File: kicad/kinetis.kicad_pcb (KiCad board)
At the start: 2 copper layers, 88.9 x 88.9 mm, 75 parts, among them J1 FTDI_Connector, J2 CONN_01X16, J3 USB_Micro_B, J4 CONN_01X16, J5 JLink_SWD_20pin, J6 CONN_01X16, J7 CONN_01X16, M1 #4-40 Mounting Hole, M2 #4-40 Mounting Hole, M3 #4-40 Mounting Hole, M4 #4-40 Mounting Hole, SW1 DPDT, SW2 SPST, SW3 SPST, SW4 SPST, SW5 SPST, SW6 SPST, U1 LM1117-ADJ, U2 MKL16Z64VLH4, Y1 12.000 MHz

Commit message: Misc tweaks
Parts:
- added C17: 0.1uF, custom_footprints:SM_0603, F.Cu at (160.8, 129.5)
- added C18: 0.1uF, custom_footprints:SM_0603, F.Cu at (172.8, 84.6)
- added C8: 0.1uF, custom_footprints:SM_0603, F.Cu at (126.8, 89.7)
- renumbered C9 to C10, C10 to C11, C11 to C12, C12 to C13, C13 to C14, C14 to C15, C15 to C16, C16 to C19, C17 to C20, C8 to C9
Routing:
- net GND: track 144.6 -> 157.0 mm, vias 53 -> 54
- net +3.3V: track 323.1 -> 334.2 mm
- net Net-(F1-Pad2): track 17.3 -> 16.4 mm
- net /HEADER_A[2]: track 24.0 -> 24.8 mm

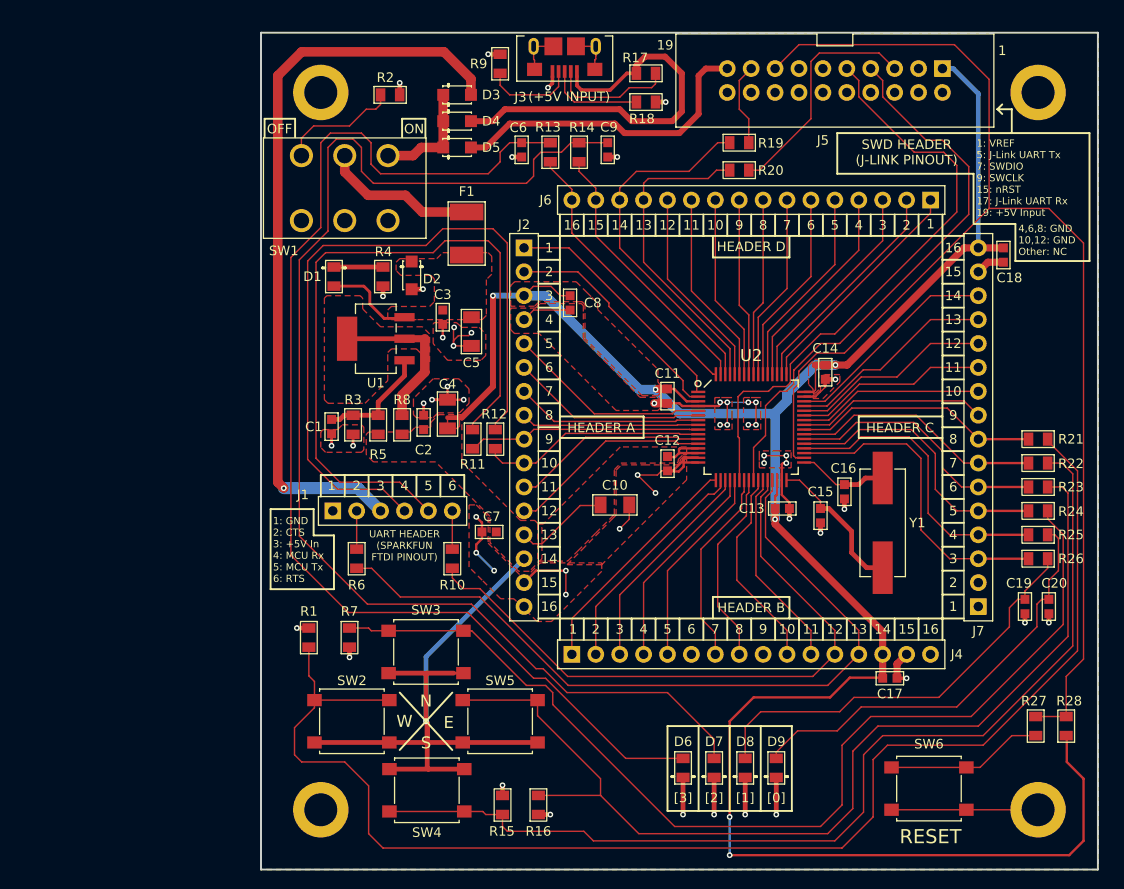
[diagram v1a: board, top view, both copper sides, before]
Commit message: Cosmetic tweaks. Added copper thieving.
This commit adds ground-referenced copper thieving to the top layer
of the PCB, and also makes a whole bunch of cosmetic changes, including
a logo on the PCB and schematic, and infoblocks for the CCA and PCB.
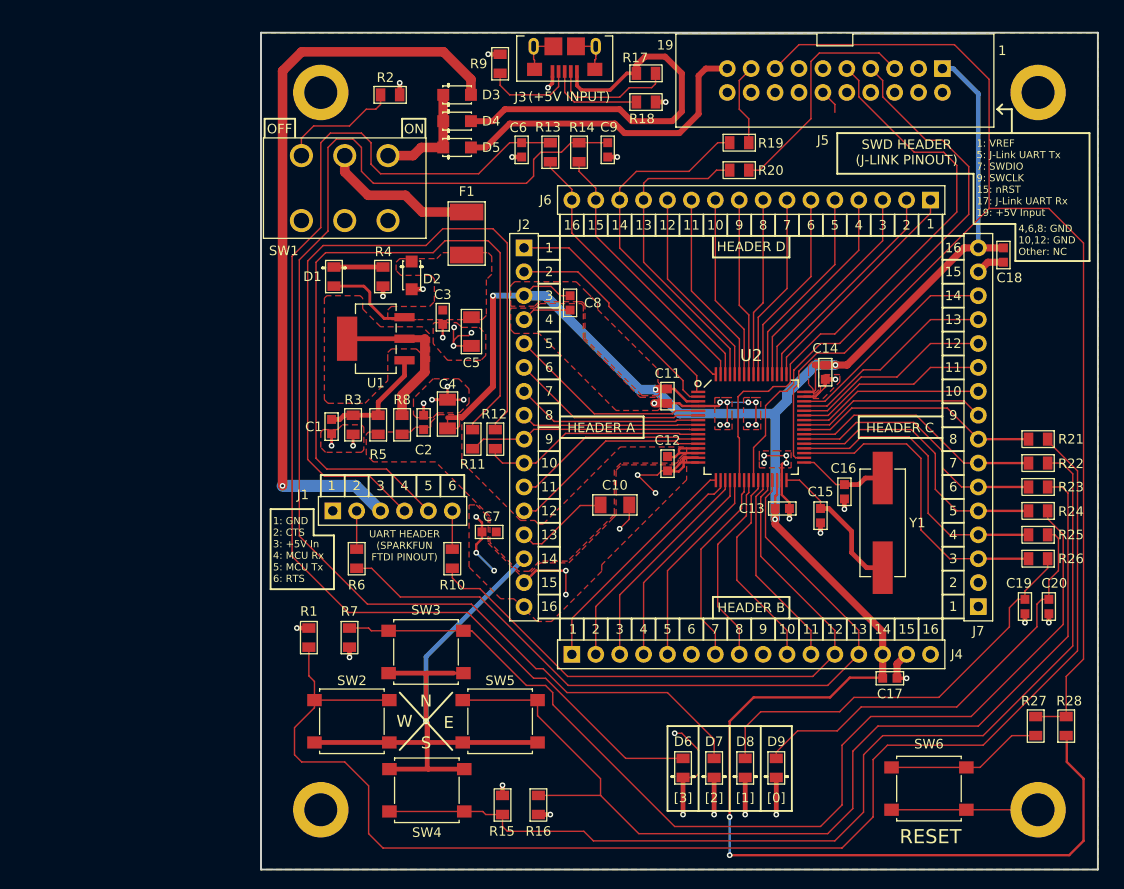
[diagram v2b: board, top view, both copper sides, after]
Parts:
- added G***: Hoboshop, custom_footprints:Hoboshop, B.Cu at (107.3, 98.4)
- added REF**: CCA_TITLE_BLOCK, custom_footprints:CCA_TITLE_BLOCK, B.Cu at (160.0, 95.9)
- added REF**: PCB_TITLE_BLOCK, custom_footprints:PCB_TITLE_BLOCK, B.Cu at (167.0, 75.6)
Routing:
- net GND: track 157.0 -> 168.4 mm, vias 54 -> 55
- net /LED[3]: track 125.6 -> 124.9 mm
- net +3.3V: track 334.2 -> 333.6 mm
- net 5V_FTDI: track 79.8 -> 79.3 mm
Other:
- rule pad_to_mask_clearance: 0.1016 -> 0.0508
- board text added: ""The Ripper" A Kinetis KL016 Evaluation Board"

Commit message: Various cosmetic tweaks
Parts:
- added G***: LOGO, custom_footprints:Signature_Mask, B.Cu at (112.5, 143.8)
- moved REF** 74.3 mm to (125.5, 137.2)
- moved REF** 38.4 mm to (172.7, 132.1)
- moved G*** 25.0 mm to (116.8, 75.3)
- moved J3 0.41 mm to (126.2, 62.8)
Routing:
- net 5V_USB: track 43.0 -> 22.5 mm
- net GND: track 168.4 -> 177.1 mm, vias 55 -> 57
- net Net-(J3-Pad2): track 12.6 -> 14.6 mm, vias 0 -> 2
- net Net-(J3-Pad3): track 9.75 -> 11.0 mm, vias 0 -> 2
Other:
- board text added: "01-001"
- board text added: "02-001"
- board text added: "1.0"
- board text added: "Flip the board over"

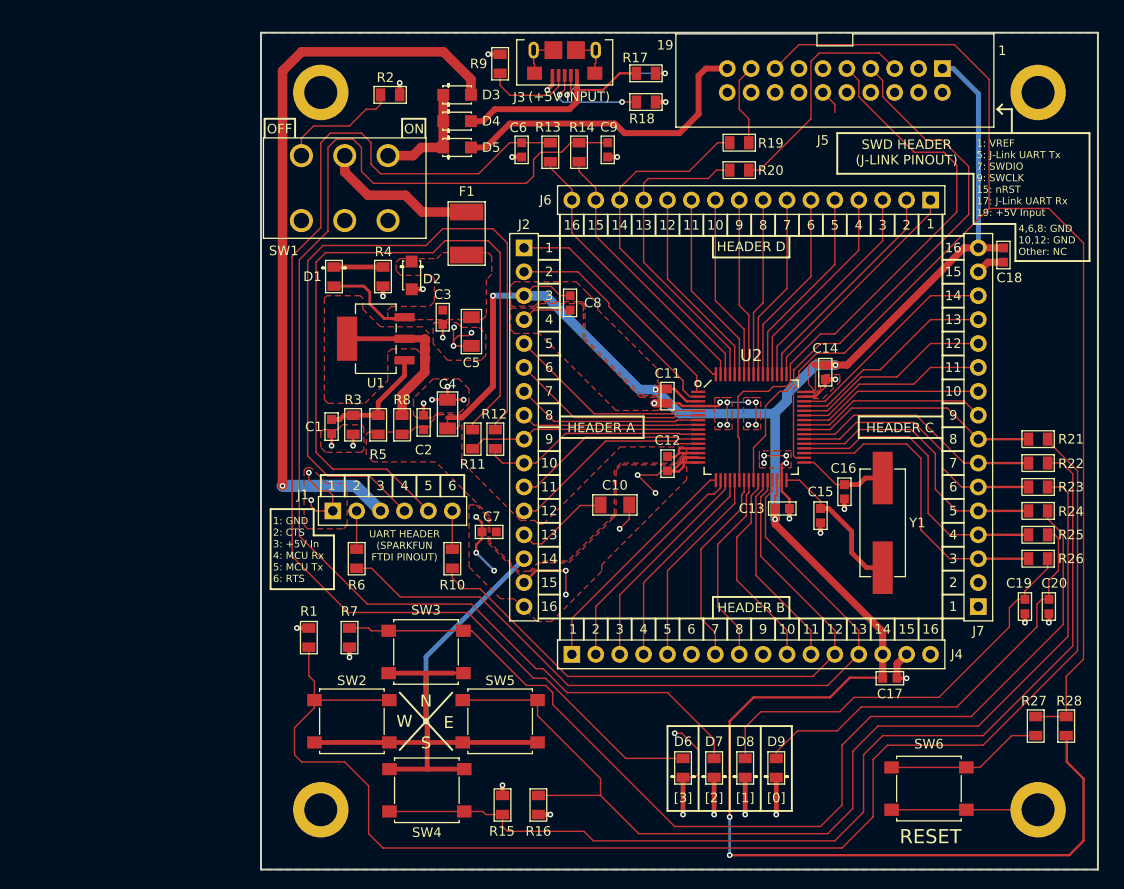
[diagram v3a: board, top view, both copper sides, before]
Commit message: Removed GND-fill pour from top side
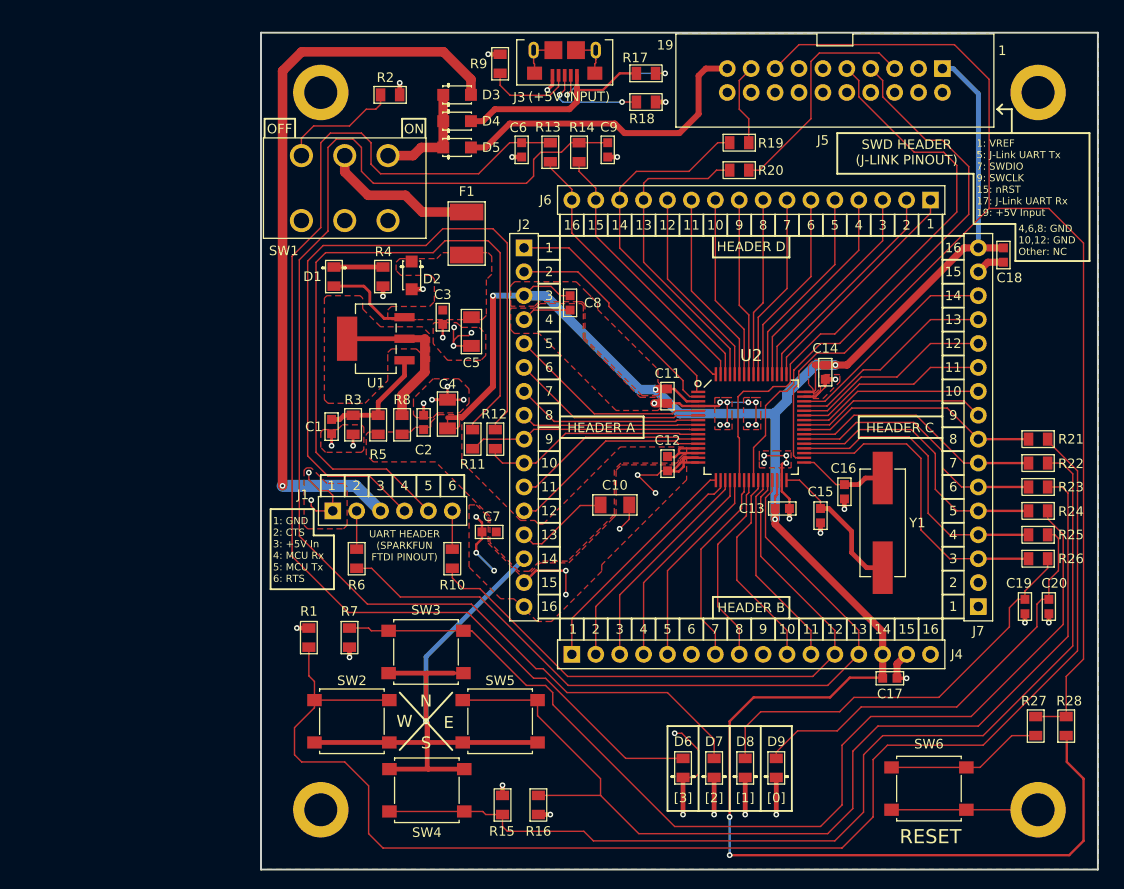
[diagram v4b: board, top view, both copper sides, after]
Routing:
- net GND: track 177.1 -> 174.5 mm
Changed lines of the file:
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@@
     (thickness 1.6002)
     (drawings 230)
-    (tracks 880)
+    (tracks 874)
     (zones 0)
     (modules 82)
@@
   (page A)
   (layers
-    (0 F.Cu signal hide)
+    (0 F.Cu signal)
     (31 B.Cu signal)
-    (33 F.Adhes user hide)
-    (35 F.Paste user hide)
+    (33 F.Adhes user)
+    (35 F.Paste user)
     (36 B.SilkS user)
-    (37 F.SilkS user hide)
+    (37 F.SilkS user)
     (38 B.Mask user)
-    (39 F.Mask user hide)
-    (40 Dwgs.User user hide)
-    (41 Cmts.User user hide)
-    (42 Eco1.User user hide)
-    (43 Eco2.User user hide)
-    (44 Edge.Cuts user hide)
-    (45 Margin user hide)
-    (47 F.CrtYd user hide)
-    (49 F.Fab user hide)
+    (39 F.Mask user)
+    (40 Dwgs.User user)
+    (41 Cmts.User user)
+    (42 Eco1.User user)
+    (43 Eco2.User user)
+    (44 Edge.Cuts user)
+    (45 Margin user)
+    (47 F.CrtYd user)
+    (49 F.Fab user)
   )
   (setup
-    (last_trace_width 0.1524)
+    (last_trace_width 0.254)
     (user_trace_width 0.1524)
     (user_trace_width 0.3048)
@@
   (gr_line (start 93.98 149.86) (end 93.98 60.96) (angle 90) (layer F.Fab) (width 0.2))
   (gr_line (start 182.88 149.86) (end 93.98 149.86) (angle 90) (layer F.Fab) (width 0.2))
-  (segment (start 124.693997 66.751191) (end 124.389198 67.05599) (width 0.381) (layer F.Cu) (net 1))
-  (segment (start 124.938 66.507188) (end 124.693997 66.751191) (width 0.381) (layer F.Cu) (net 1))
-  (segment (start 124.938 66.0164) (end 124.938 66.507188) (width 0.381) (layer F.Cu) (net 1))
+  (segment (start 124.938 66.507188) (end 124.389198 67.05599) (width 0.381) (layer F.Cu) (net 1))
+  (segment (start 124.938 66.0164) (end 124.938 66.507188) (width 0.381) (layer F.Cu) (net 1) (status 10))
   (via (at 124.389198 67.05599) (size 0.6096) (drill 0.3048) (layers F.Cu B.Cu) (net 1))
-  (segment (start 150.114 111.506) (end 150.114 110.49) (width 0.254) (layer F.Cu) (net 1))
+  (segment (start 150.114 111.506) (end 150.114 110.49) (width 0.254) (layer F.Cu) (net 1) (status 10))
   (segment (start 150.114 110.49) (end 149.3 109.676) (width 0.254) (layer F.Cu) (net 1))
-  (segment (start 149.3 109.676) (end 149.3 108.495) (width 0.254) (layer F.Cu) (net 1))
+  (segment (start 149.3 109.676) (end 149.3 108.495) (width 0.254) (layer F.Cu) (net 1) (status 20))
   (segment (start 99.822 111.76) (end 99.314 111.252) (width 0.1524) (layer F.Cu) (net 1))
   (segment (start 99.314 111.252) (end 99.314 110.617) (width 0.1524) (layer F.Cu) (net 1))
@@
   (segment (start 152.9068 99.62) (end 153.3652 99.1616) (width 0.1524) (layer F.Cu) (net 1))
   (segment (start 153.924 98.3488) (end 153.924 97.79) (width 0.254) (layer F.Cu) (net 1) (status 20))
-  (segment (start 154.94 68.58) (end 154.94 69.418948) (width 0.1524) (layer F.Cu) (net 1))
-  (segment (start 153.67 67.31) (end 154.94 68.58) (width 0.1524) (layer F.Cu) (net 1) (status 10))
   (segment (start 152.9068 99.62) (end 153.924 98.6028) (width 0.1524) (layer F.Cu) (net 1))
   (segment (start 153.924 98.6028) (end 153.924 97.79) (width 0.254) (layer F.Cu) (net 1) (status 20))
@@
   (segment (start 126.746 69.088) (end 118.8212 69.088) (width 0.635) (layer F.Cu) (net 10))
   (segment (start 118.8212 69.088) (end 117.5512 70.358) (width 0.635) (layer F.Cu) (net 10))
-  (segment (start 117.5512 70.358) (end 116.2812 70.358) (width 0.635) (layer F.Cu) (net 10))
+  (segment (start 117.5512 70.358) (end 116.2812 70.358) (width 0.635) (layer F.Cu) (net 10) (status 20))
   (segment (start 127.538 66.832) (end 127.546102 66.840102) (width 0.635) (layer F.Cu) (net 10))
   (segment (start 127.546102 66.840102) (end 127.546102 68.287898) (width 0.635) (layer F.Cu) (net 10))
   (segment (start 127.546102 68.287898) (end 126.746 69.088) (width 0.635) (layer F.Cu) (net 10))
-  (segment (start 133.858 65.278) (end 132.08 65.278) (width 0.254) (layer F.Cu) (net 10))
+  (segment (start 133.858 65.278) (end 132.08 65.278) (width 0.254) (layer F.Cu) (net 10) (status 10))
   (segment (start 132.08 65.278) (end 130.302 67.056) (width 0.254) (layer F.Cu) (net 10))
   (segment (start 130.302 67.056) (end 127.538 67.056) (width 0.254) (layer F.Cu) (net 10))
   (segment (start 127.538 67.056) (end 127.538 66.548) (width 0.254) (layer F.Cu) (net 10))
-  (segment (start 127.538 66.294) (end 127.538 66.548) (width 0.381) (layer F.Cu) (net 10))
+  (segment (start 127.538 65.4892) (end 127.538 66.548) (width 0.381) (layer F.Cu) (net 10) (status 10))
   (segment (start 127.538 66.548) (end 127.538 66.832) (width 0.381) (layer F.Cu) (net 10))
-  (segment (start 127.538 65.4892) (end 127.538 66.294) (width 0.381) (layer F.Cu) (net 10))
   (segment (start 104.013 109.093) (end 96.266 109.093) (width 1.27) (layer B.Cu) (net 11))
   (segment (start 106.68 111.76) (end 104.013 109.093) (width 1.27) (layer B.Cu) (net 11) (status 10))
@@
   (segment (start 130.81 66.548) (end 132.08 65.278) (width 0.1524) (layer B.Cu) (net 70))
   (segment (start 132.08 65.278) (end 136.906 65.278) (width 0.1524) (layer B.Cu) (net 70))
-  (segment (start 136.906 65.278) (end 135.89 65.278) (width 0.1524) (layer F.Cu) (net 70))
+  (segment (start 136.906 65.278) (end 135.89 65.278) (width 0.1524) (layer F.Cu) (net 70) (status 20))
   (via (at 136.906 65.278) (size 0.6096) (drill 0.3048) (layers F.Cu B.Cu) (net 70))
-  (segment (start 126.798231 67.260633) (end 126.493432 67.565432) (width 0.1524) (layer F.Cu) (net 70))
+  (segment (start 126.888 67.170864) (end 126.493432 67.565432) (width 0.1524) (layer F.Cu) (net 70))
   (via (at 126.493432 67.565432) (size 0.6096) (drill 0.3048) (layers F.Cu B.Cu) (net 70))
-  (segment (start 126.888 67.170864) (end 126.798231 67.260633) (width 0.1524) (layer F.Cu) (net 70))
-  (segment (start 126.888 65.4892) (end 126.888 67.170864) (width 0.1524) (layer F.Cu) (net 70))
+  (segment (start 126.888 65.4892) (end 126.888 67.170864) (width 0.1524) (layer F.Cu) (net 70) (status 10))
   (segment (start 125.704587 67.564) (end 125.704587 67.995052) (width 0.1524) (layer B.Cu) (net 71))
   (segment (start 125.704587 67.995052) (end 126.035535 68.326) (width 0.1524) (layer B.Cu) (net 71))
   (segment (start 126.035535 68.326) (end 132.334 68.326) (width 0.1524) (layer B.Cu) (net 71))
-  (segment (start 132.334 68.326) (end 133.858 68.326) (width 0.1524) (layer F.Cu) (net 71))
+  (segment (start 132.334 68.326) (end 133.858 68.326) (width 0.1524) (layer F.Cu) (net 71) (status 20))
   (via (at 132.334 68.326) (size 0.6096) (drill 0.3048) (layers F.Cu B.Cu) (net 71))
-  (segment (start 126.238 65.4892) (end 126.238 67.030587) (width 0.1524) (layer F.Cu) (net 71))
-  (segment (start 126.238 67.030587) (end 126.009386 67.259201) (width 0.1524) (layer F.Cu) (net 71))
-  (segment (start 126.009386 67.259201) (end 125.704587 67.564) (width 0.1524) (layer F.Cu) (net 71))
+  (segment (start 126.238 65.4892) (end 126.238 67.030587) (width 0.1524) (layer F.Cu) (net 71) (status 10))
+  (segment (start 126.238 67.030587) (end 125.704587 67.564) (width 0.1524) (layer F.Cu) (net 71))
   (via (at 125.704587 67.564) (size 0.6096) (drill 0.3048) (layers F.Cu B.Cu) (net 71))
-  (segment (start 119.38 65.278) (end 119.38 66.548) (width 0.1524) (layer F.Cu) (net 72))
+  (segment (start 119.38 65.278) (end 119.38 66.548) (width 0.1524) (layer F.Cu) (net 72) (status 10))
   (segment (start 119.38 66.548) (end 120.4468 67.6148) (width 0.1524) (layer F.Cu) (net 72))
   (segment (start 120.4468 67.6148) (end 124.6632 67.6148) (width 0.1524) (layer F.Cu) (net 72))
   (segment (start 124.6632 67.6148) (end 125.5945 66.6835) (width 0.1524) (layer F.Cu) (net 72))
-  (segment (start 125.5945 66.6835) (end 125.5945 66.0099) (width 0.1524) (layer F.Cu) (net 72))
+  (segment (start 125.5945 66.6835) (end 125.5945 66.0099) (width 0.1524) (layer F.Cu) (net 72) (status 20))
   (segment (start 104.14 111.76) (end 104.14 115.824) (width 0.1524) (layer F.Cu) (net 73) (status 30))
   (segment (start 118.872 103.124) (end 118.872 102.4636) (width 0.1524) (layer F.Cu) (net 74) (status 10))
@@
       )
     )
-  )
-  (zone (net 1) (net_name GND) (layer F.Cu) (hatch edge 0.508)
-    (connect_pads (clearance 0.762))
-    (min_thickness 0.254)
-    (fill yes (mode segment) (arc_segments 32) (thermal_gap 0.635) (thermal_bridge_width 0.508))
-    (polygon
-      (pts
-        (xy 182.88 60.96) (xy 182.88 149.86) (xy 93.98 149.86) (xy 93.98 60.96)
-      )
-    )

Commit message: Added some more copper. Changed vias to 0.014"/0.032".
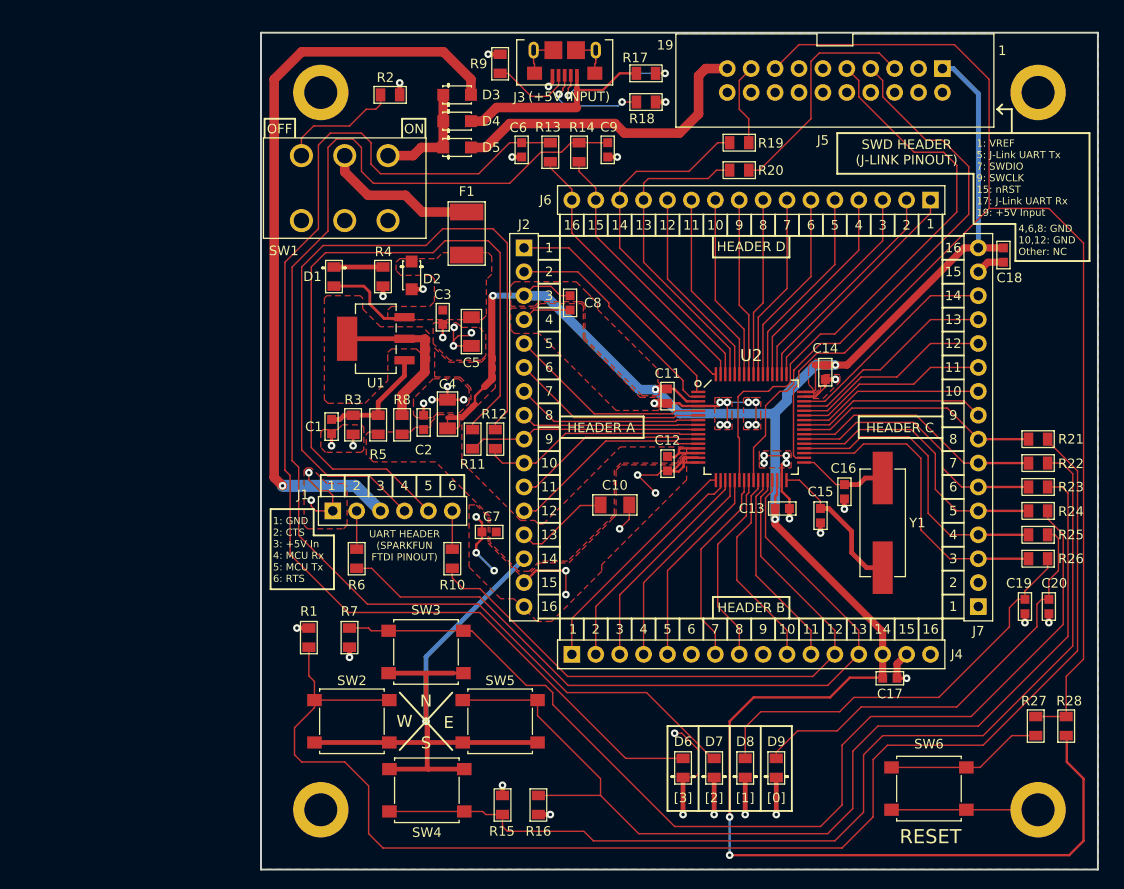
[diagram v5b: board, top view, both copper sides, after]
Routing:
- net /LED[2]: track 133.9 -> 132.3 mm
- net 5V_FTDI: track 79.3 -> 80.0 mm
- net Net-(J3-Pad4): track 8.99 -> 8.25 mm
- net /LED[3]: track 124.9 -> 125.6 mm
- net TXD_FTDI: track 77.0 -> 77.5 mm
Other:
- net class Default: via_dia 0.6096 -> 0.8128; via_drill 0.3048 -> 0.3556
- rule via_min_drill: 0.3048 -> 0.3556
- rule via_min_size: 0.6096 -> 0.8128

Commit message: Adde a shitload of copper
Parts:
- moved J5 1.80 mm to (165.1, 66.0)
- moved R19 0.76 mm to (144.8, 73.4)
- moved R17 0.51 mm to (134.4, 65.3)
- moved R18 0.51 mm to (134.4, 68.3)
- moved R20 0.23 mm to (144.8, 75.8)
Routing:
- net GND: track 174.0 -> 473.9 mm, vias 57 -> 89
- net (no net): track 0.00 -> 26.5 mm
- net 5V_JLink: track 33.9 -> 30.8 mm
- net Net-(J3-Pad2): track 14.5 -> 17.6 mm
- net JLink_nRST: track 142.7 -> 144.9 mm
- net JLink_SWCLK: track 63.4 -> 64.9 mm
- net Net-(J3-Pad3): track 11.5 -> 10.0 mm
- net JLink_SWDIO: track 60.1 -> 61.4 mm
- net RXD_FTDI: track 76.2 -> 75.0 mm
- net Net-(J3-Pad4): track 8.25 -> 9.33 mm
- net +3.3V: track 333.6 -> 334.5 mm
- net JLink_Rx: track 8.82 -> 8.01 mm
- net /LED[2]: track 132.3 -> 131.5 mm
